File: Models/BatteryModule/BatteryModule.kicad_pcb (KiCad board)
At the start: 2 copper layers, 86.4 x 27.6 mm, 8 parts, among them J1 Conn_01x02_Pin, J2 Conn_01x02_Pin, J3 Keystone_968, J4 Keystone_968, J5 Keystone_968, J6 Keystone_968, J7 Conn_01x02_Pin, J8 Conn_01x02_Pin

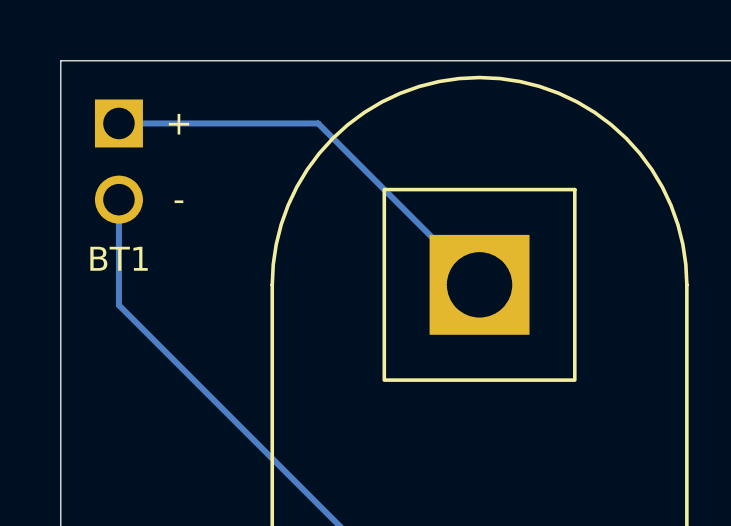
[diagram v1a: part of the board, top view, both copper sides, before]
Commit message: Polarized the battery module by offsetting one of the pin headers
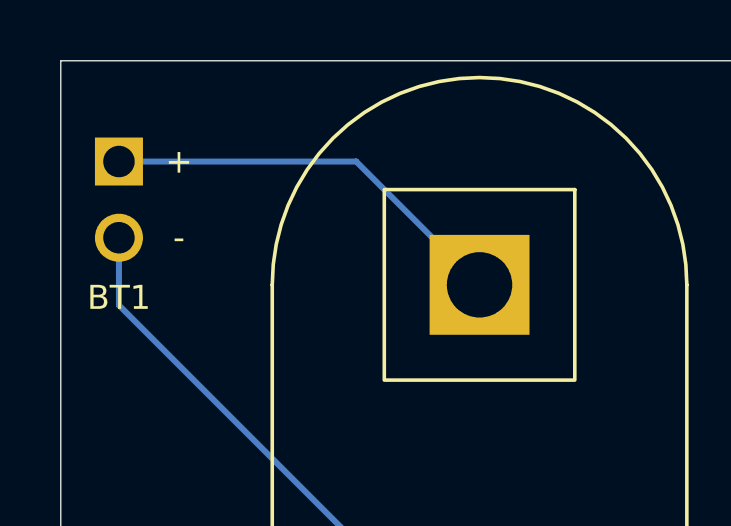
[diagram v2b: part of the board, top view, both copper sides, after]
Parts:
- moved J1 1.27 mm to (110.5, 91.0)
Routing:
- net Net-(J1-Pin_2): track 20.5 -> 19.2 mm
- net Net-(J1-Pin_1): track 14.2 -> 13.7 mm
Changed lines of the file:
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@@
 		(locked yes)
 		(layer "B.Cu")
-		(at 110.46 89.7 180)
+		(at 110.46 90.97 180)
 		(property "Reference" "J1"
 			(at 0.07 3.78 0)
@@
 	)
 	(gr_text "BT1"
-		(at 110.46 92.97 0)
+		(at 110.46 94.24 0)
 		(layer "F.SilkS")
 		(effects
@@
 	)
 	(gr_text "-"
-		(at 112.46 90.97 0)
+		(at 112.46 92.24 0)
 		(layer "F.SilkS")
 		(effects
@@
 	)
 	(gr_text "+"
-		(at 112.46 88.43 0)
+		(at 112.46 89.7 0)
 		(layer "F.SilkS")
 		(effects
@@
 	)
 	(segment
-		(start 117.1 88.43)
+		(start 110.46 89.7)
+		(end 118.37 89.7)
+		(width 0.2)
+		(layer "B.Cu")
+		(net 1)
+	)
+	(segment
+		(start 118.37 89.7)
 		(end 122.48 93.81)
 		(width 0.2)
 		(layer "B.Cu")
 		(net 1)
-	)
-	(segment
-		(start 110.46 88.43)
-		(end 117.1 88.43)
-		(width 0.2)
-		(layer "B.Cu")
-		(net 1)
-	)
-	(segment
-		(start 110.46 94.49)
-		(end 110.46 90.97)
-		(width 0.2)
-		(layer "B.Cu")
-		(net 2)
 	)
 	(segment
@@
 		(width 0.2)
 		(layer "B.Cu")
+		(net 2)
+	)
+	(segment
+		(start 110.46 94.49)
+		(end 110.46 92.24)
+		(width 0.2)
+		(layer "B.Cu")

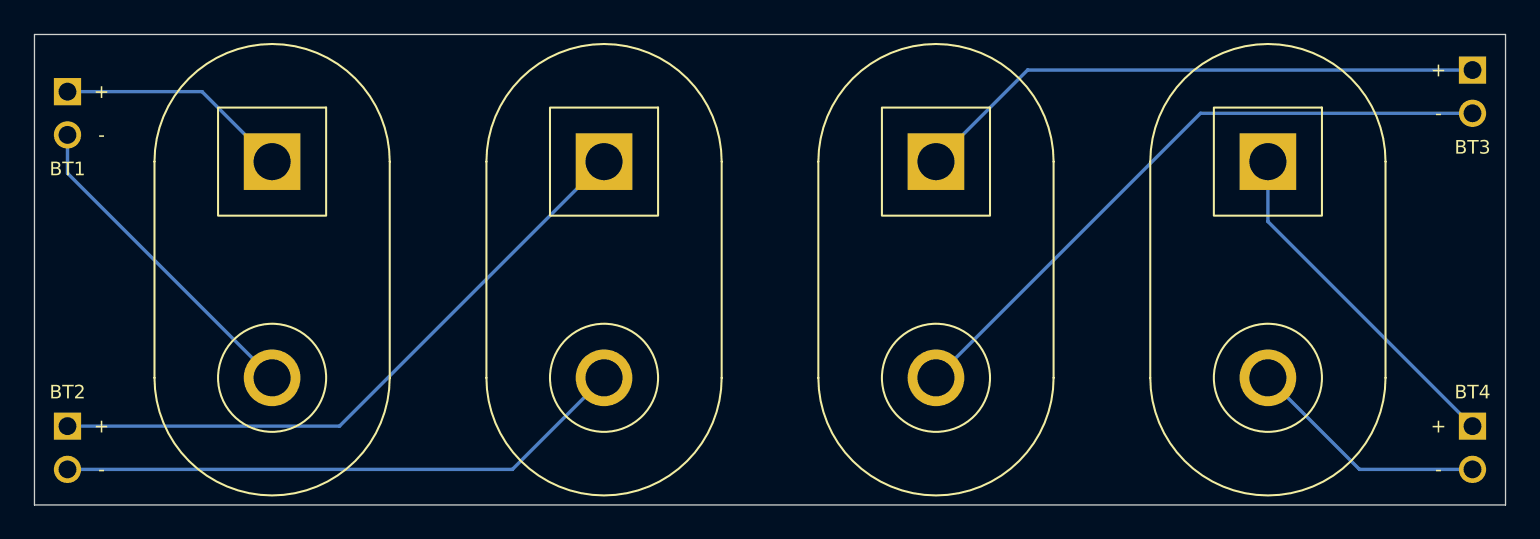
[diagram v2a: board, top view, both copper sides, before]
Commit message: Fixed some of the silkscreen for the battery module
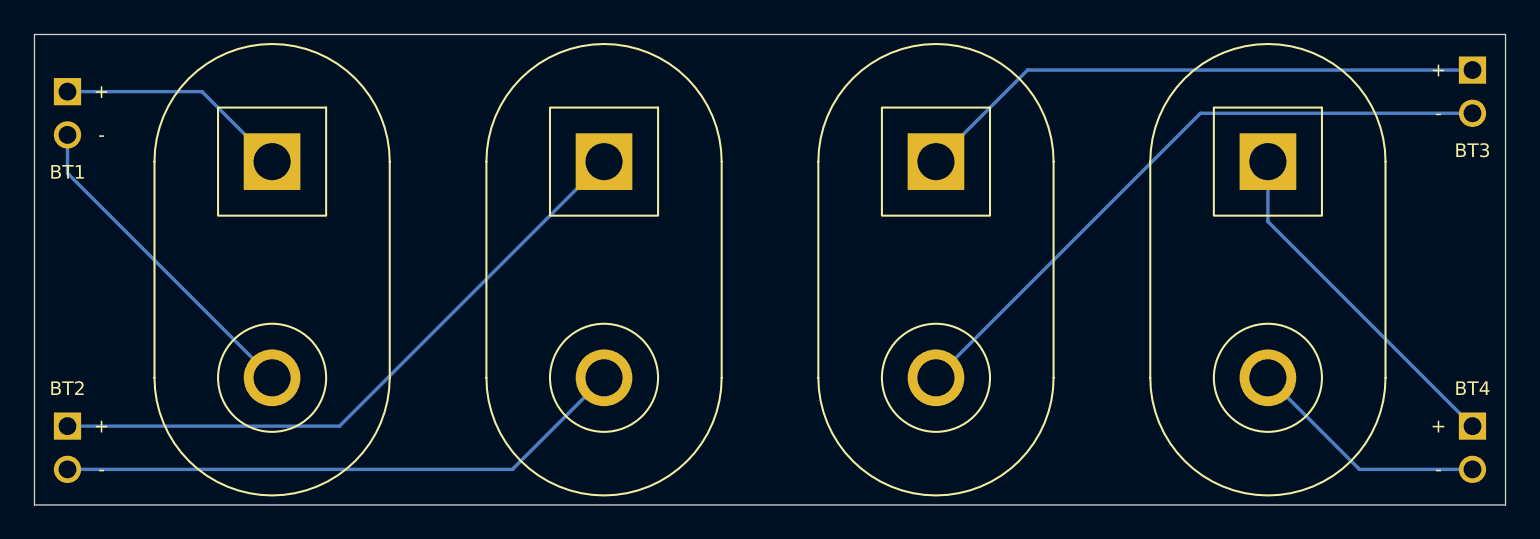
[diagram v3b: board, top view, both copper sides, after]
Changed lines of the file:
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@@
 	)
 	(gr_text "BT1"
-		(at 110.46 94.24 0)
+		(at 110.46 94.44 0)
 		(layer "F.SilkS")
 		(effects
@@
 	)
 	(gr_text "BT2"
-		(at 110.46 107.35 0)
+		(at 110.46 107.15 0)
 		(layer "F.SilkS")
 		(effects
@@
 	)
 	(gr_text "BT3"
-		(at 193 92.97 0)
+		(at 193 93.17 0)
 		(layer "F.SilkS")
 		(effects
@@
 	)
 	(gr_text "BT4"
-		(at 193 107.35 0)
+		(at 193 107.15 0)
 		(layer "F.SilkS")
 		(effects
